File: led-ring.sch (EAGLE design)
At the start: 29 parts, among them IC8 MCP23017, X1 78127-1128, X2 78127-1128

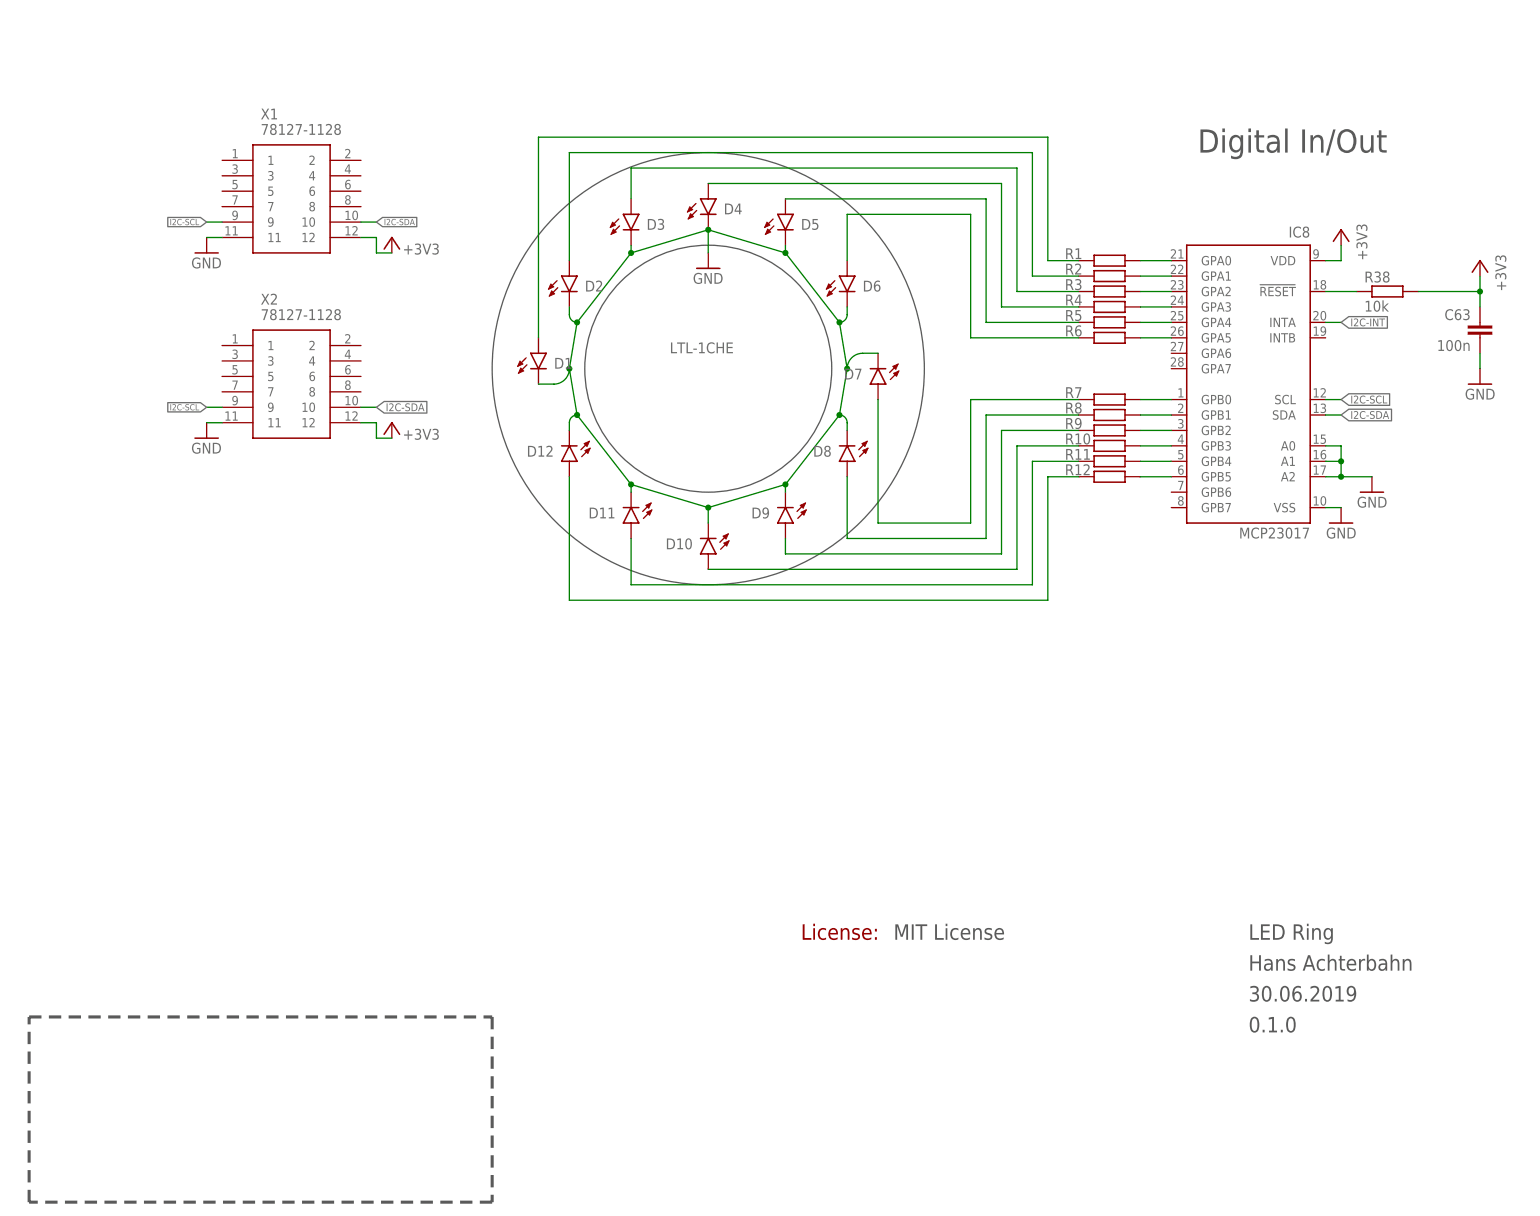
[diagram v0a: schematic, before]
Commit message: beautified schematic | added i2c pull up resistors | beauty corrections on the board
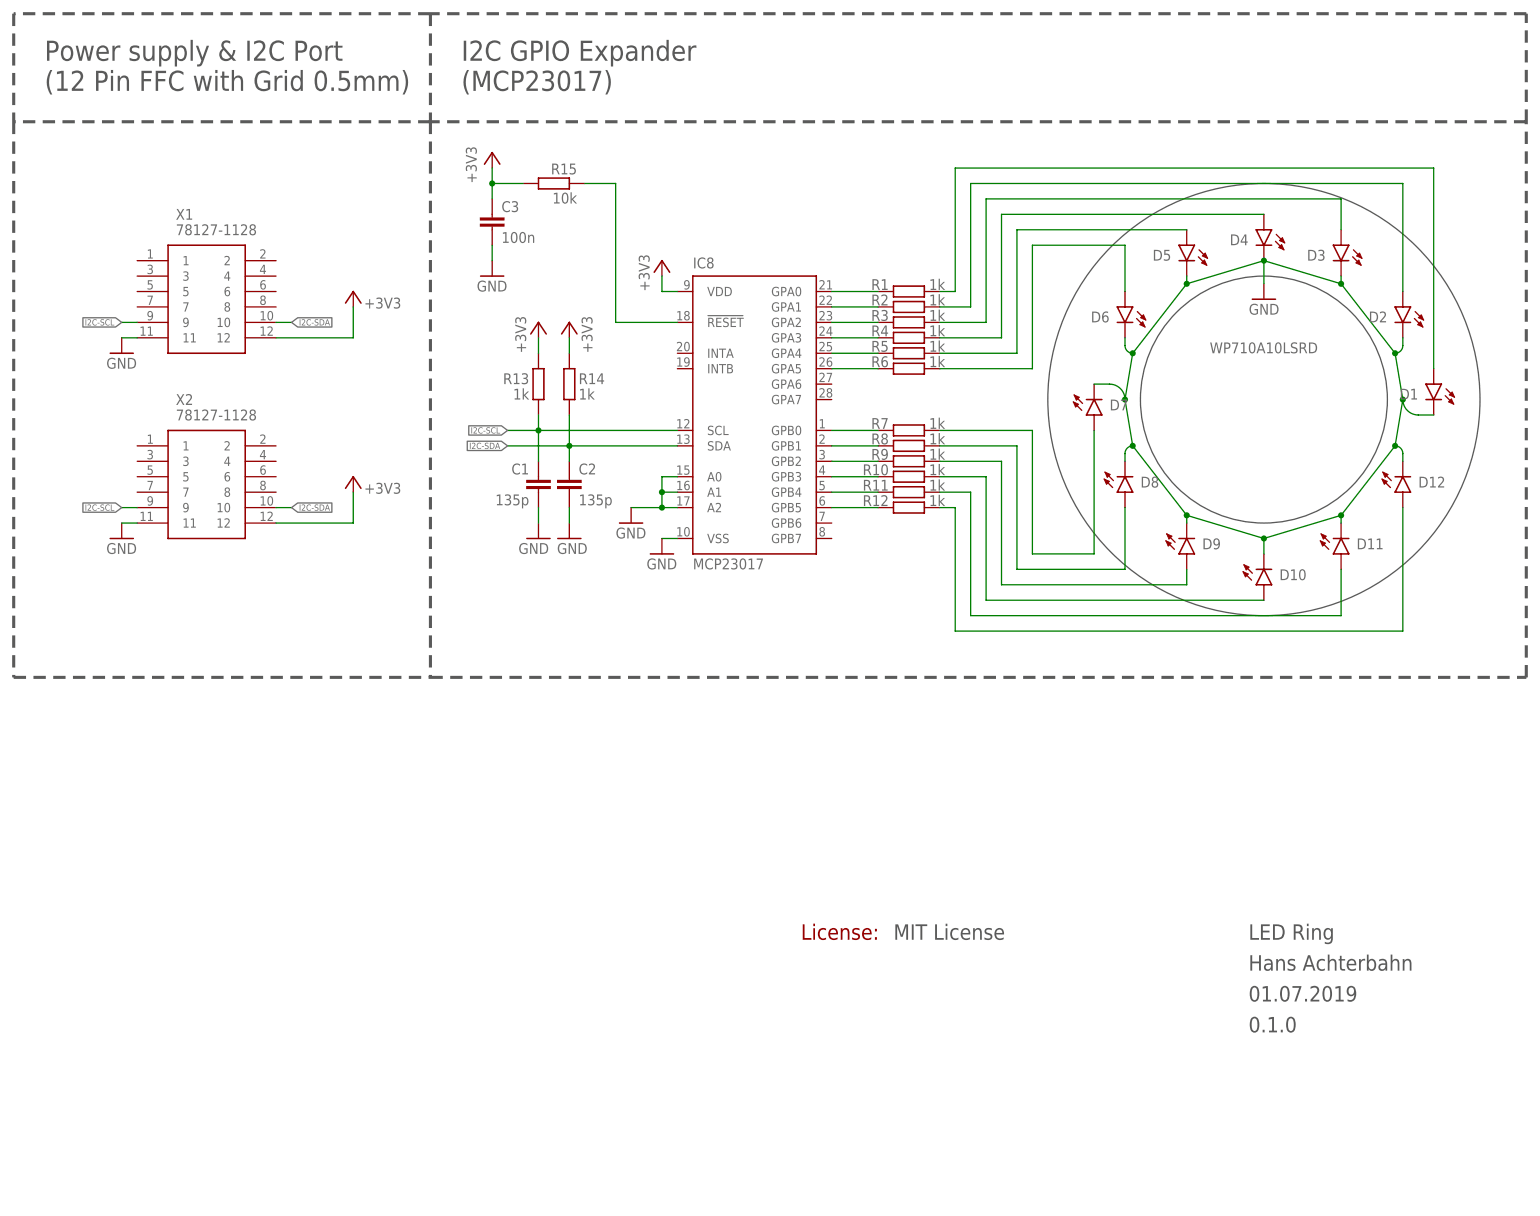
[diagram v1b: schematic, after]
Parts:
- removed C63: 100n, rcl:C-EUC0603
- removed R38: 10k, rcl:R-EU_R0603
- added C1, C2: 135p, rcl:C-EUC0603
- added C3: 100n, rcl:C-EUC0603
- added R13, R14: 1k, rcl:R-EU_R0603
- added R15: 10k, rcl:R-EU_R0603
- D1, D10, D11, D12, D2, D3, D4, D5, D6, D7, D8, D9: value LTL-1CHE -> WP710A10LSRD
- R1, R10, R11, R12, R2, R3, R4, R5, R6, R7, R8, R9: value (none) -> 1k
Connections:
- removed net I2C-INT: IC8.INTA
- net +3V3: now also C3.1, R13.1, R14.1, R15.2; no longer C63.1, R38.2
- net GND: now also C1.2, C2.2, C3.2; no longer C63.2
- net I2C-SCL: now also C1.1, R13.2
- net I2C-SDA: now also C2.1, R14.2
- net N$213: now also R15.1; no longer R38.1
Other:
- note added: "I2C GPIO Expander (MCP23017)"
- note added: "Power supply & I2C Port (12 Pin FFC with Grid 0.5mm)"
- note removed: "Digital In/Out"
- moved on the sheet: D1, D10, D11, D12, D2, D3, D4, D5, D6, D7, D8, D9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
